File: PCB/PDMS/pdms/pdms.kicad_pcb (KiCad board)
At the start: 2 copper layers, 104 parts, among them IC1 BTS500101TAEATMA1, IC12 TMP126NDCKR, IC13 TMP126NDCKR, IC14 TMP126NDCKR, IC2 BTS500101TAEATMA1, IC3 BTS500101TAEATMA1, IC4 BTS500101TAEATMA1, IC5 BTS500101TAEATMA1, IC6 BTS500101TAEATMA1, IC7 BTS722204ESAXUMA1, IC8 BTS500101TAEATMA1, IC9 BTS500101TAEATMA1, J1 DBG, Q1 AO3401A, Q2 MMBT3904, U1 STM32F405RGTx, U2 MCP2561-E-SN, U3 MCP2561-E-SN, Y1 16Mhz, Y2 32KHz

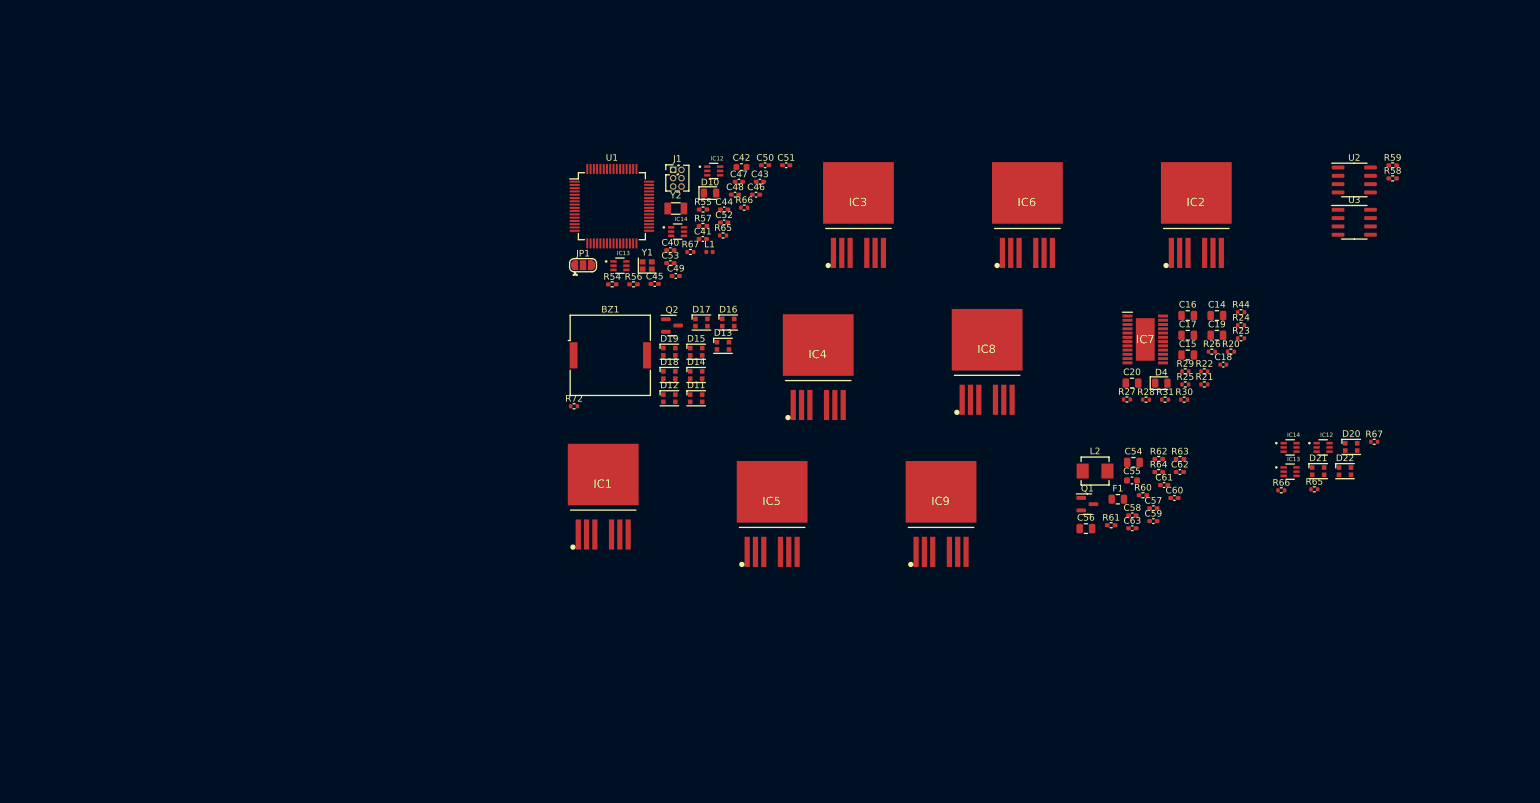
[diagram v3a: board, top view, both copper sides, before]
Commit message: Added ADC overvoltage protection
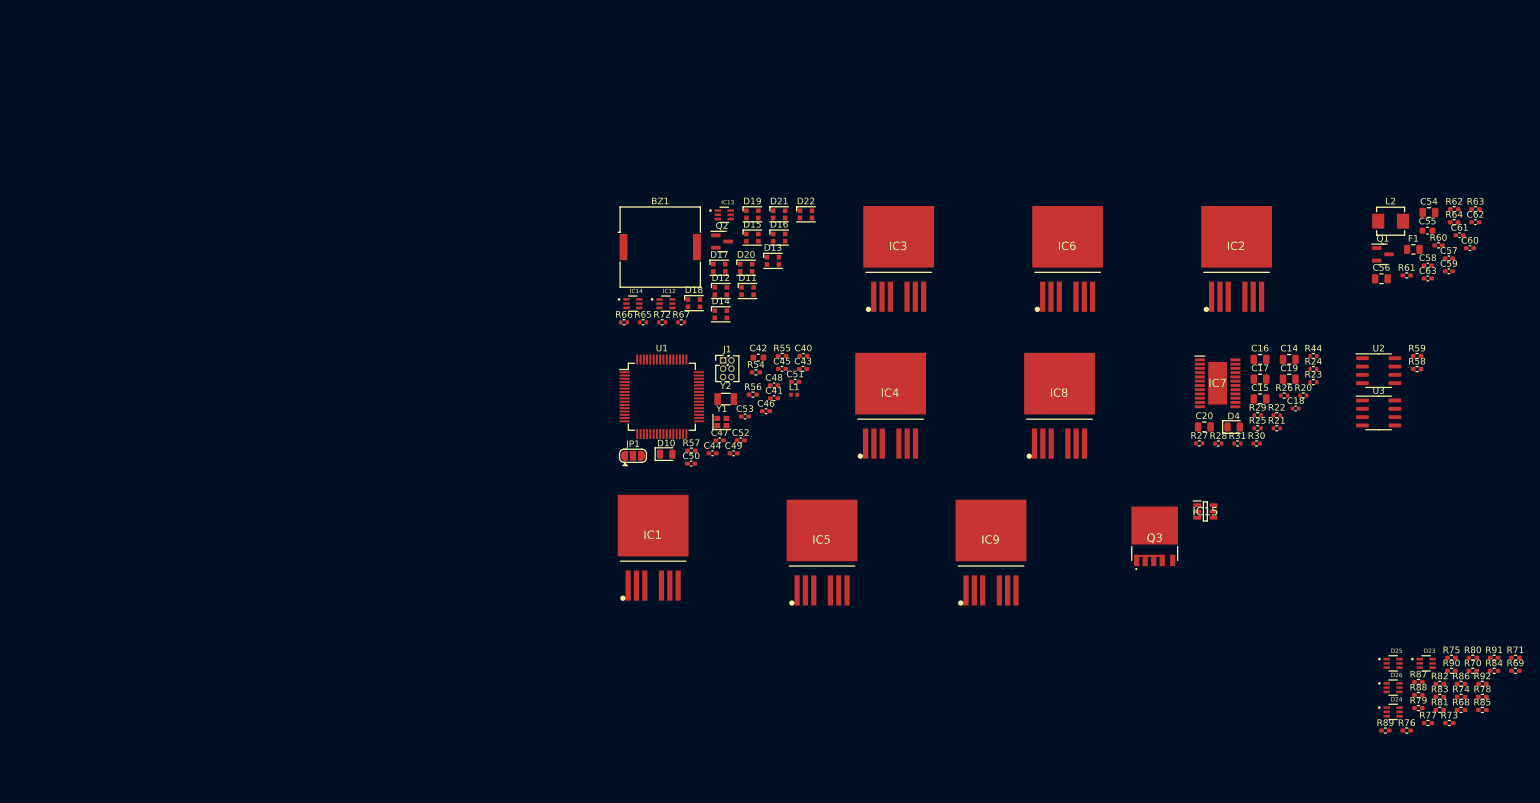
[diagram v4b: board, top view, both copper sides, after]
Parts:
- removed the IC12 at (128.8, 37.9)
- removed the IC12 at (221.8, 80.1)
- removed the IC13 at (114.5, 52.4)
- removed the IC13 at (216.7, 83.8)
- removed the IC14 at (123.3, 47.2)
- removed the IC14 at (216.7, 80.1)
- removed the R65 at (220.4, 86.5)
- removed the R65 at (130.2, 47.8)
- removed the R66 at (133.5, 43.5)
- removed the R66 at (215.4, 86.6)
- removed the R67 at (229.6, 79.2)
- removed the R67 at (125.3, 50.3)
- added D23: BAT54BRW-7-F, PDM_Additional:SOT65P210X110-6N, F.Cu at (237.5, 113.0)
- added D24: BAT54BRW-7-F, PDM_Additional:SOT65P210X110-6N, F.Cu at (232.4, 120.4)
- added D25: BAT54BRW-7-F, PDM_Additional:SOT65P210X110-6N, F.Cu at (232.4, 113.0)
- added D26: BAT54BRW-7-F, PDM_Additional:SOT65P210X110-6N, F.Cu at (232.4, 116.7)
- added IC12: TMP126NDCKR, PDM_Additional:SOT65P210X110-6N, F.Cu at (121.5, 58.2)
- added IC13: TMP126NDCKR, PDM_Additional:SOT65P210X110-6N, F.Cu at (130.4, 44.6)
- added IC14: TMP126NDCKR, PDM_Additional:SOT65P210X110-6N, F.Cu at (116.5, 58.2)
- added IC15: LM74700QDBVRQ1, PDMS_Additional:SOT95P280X145-6N, F.Cu at (203.8, 89.9)
- added Q3: IAUA250N04S6N007AUMA1, PDM_Additional:IAUA250N04S6N007AUMA1, F.Cu at (196.1, 94.9)
- added R65: 10k, Resistor_SMD:R_0402_1005Metric, F.Cu at (118.0, 61.0)
- added R66: 10k, Resistor_SMD:R_0402_1005Metric, F.Cu at (115.1, 61.0)
- added R67: 10k, Resistor_SMD:R_0402_1005Metric, F.Cu at (123.9, 61.0)
- added R68: 1.2k, Resistor_SMD:R_0402_1005Metric_Pad0.72x0.64mm_HandSolder, F.Cu at (242.8, 120.1)
- added R69: 2.2k, Resistor_SMD:R_0402_1005Metric_Pad0.72x0.64mm_HandSolder, F.Cu at (251.1, 114.2)
- added R70: 1.2k, Resistor_SMD:R_0402_1005Metric_Pad0.72x0.64mm_HandSolder, F.Cu at (244.6, 114.2)
- added R71: 2.2k, Resistor_SMD:R_0402_1005Metric_Pad0.72x0.64mm_HandSolder, F.Cu at (251.1, 112.2)
- added R73: 249, Resistor_SMD:R_0402_1005Metric_Pad0.72x0.64mm_HandSolder, F.Cu at (241.0, 122.1)
- added R74: 249, Resistor_SMD:R_0402_1005Metric_Pad0.72x0.64mm_HandSolder, F.Cu at (242.8, 118.1)
- added R75: 1.2k, Resistor_SMD:R_0402_1005Metric_Pad0.72x0.64mm_HandSolder, F.Cu at (241.4, 112.2)
- added R76: 2.2k, Resistor_SMD:R_0402_1005Metric_Pad0.72x0.64mm_HandSolder, F.Cu at (234.5, 123.3)
- added R77: 1.2k, Resistor_SMD:R_0402_1005Metric_Pad0.72x0.64mm_HandSolder, F.Cu at (237.8, 122.1)
- added R78: 2.2k, Resistor_SMD:R_0402_1005Metric_Pad0.72x0.64mm_HandSolder, F.Cu at (246.1, 118.1)
- added R79: 1.2k, Resistor_SMD:R_0402_1005Metric_Pad0.72x0.64mm_HandSolder, F.Cu at (236.3, 119.9)
- added R80: 2.2k, Resistor_SMD:R_0402_1005Metric_Pad0.72x0.64mm_HandSolder, F.Cu at (244.6, 112.2)
- added R81: 1.2k, Resistor_SMD:R_0402_1005Metric_Pad0.72x0.64mm_HandSolder, F.Cu at (239.6, 120.1)
- added R82: 2.2k, Resistor_SMD:R_0402_1005Metric_Pad0.72x0.64mm_HandSolder, F.Cu at (239.6, 116.2)
- added R83: 1.2k, Resistor_SMD:R_0402_1005Metric_Pad0.72x0.64mm_HandSolder, F.Cu at (239.6, 118.1)
- added R84: 2.2k, Resistor_SMD:R_0402_1005Metric_Pad0.72x0.64mm_HandSolder, F.Cu at (247.9, 114.2)
- added R85: 1.2k, Resistor_SMD:R_0402_1005Metric_Pad0.72x0.64mm_HandSolder, F.Cu at (246.1, 120.1)
- added R86: 2.2k, Resistor_SMD:R_0402_1005Metric_Pad0.72x0.64mm_HandSolder, F.Cu at (242.8, 116.2)
- added R87: 249, Resistor_SMD:R_0402_1005Metric_Pad0.72x0.64mm_HandSolder, F.Cu at (236.3, 115.9)
- added R88: 249, Resistor_SMD:R_0402_1005Metric_Pad0.72x0.64mm_HandSolder, F.Cu at (236.3, 117.9)
- added R89: 249, Resistor_SMD:R_0402_1005Metric_Pad0.72x0.64mm_HandSolder, F.Cu at (231.3, 123.3)
- added R90: 249, Resistor_SMD:R_0402_1005Metric_Pad0.72x0.64mm_HandSolder, F.Cu at (241.4, 114.2)
- added R91: 249, Resistor_SMD:R_0402_1005Metric_Pad0.72x0.64mm_HandSolder, F.Cu at (247.9, 112.2)
- added R92: 249, Resistor_SMD:R_0402_1005Metric_Pad0.72x0.64mm_HandSolder, F.Cu at (246.1, 116.2)
- moved D20 96.3 mm to (133.8, 52.7)
- moved D21 91.1 mm to (138.8, 44.5)
- moved D22 91.1 mm to (142.9, 44.5)
- moved C57 59.0 mm to (241.0, 51.2)
- moved C58 59.0 mm to (237.7, 52.3)
- moved C59 59.0 mm to (241.0, 53.2)
- moved C61 59.0 mm to (242.6, 47.7)
- moved C62 59.0 mm to (245.0, 45.7)
- moved C63 59.0 mm to (237.7, 54.3)
- moved R60 59.0 mm to (239.4, 49.3)
- moved C54 59.0 mm to (237.9, 44.3)
- moved C55 59.0 mm to (237.7, 47.0)
- moved C56 59.0 mm to (230.7, 54.4)
- moved C60 59.0 mm to (244.2, 49.7)
- moved F1 59.0 mm to (235.5, 49.9)
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
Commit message: Added CAN ESD protection
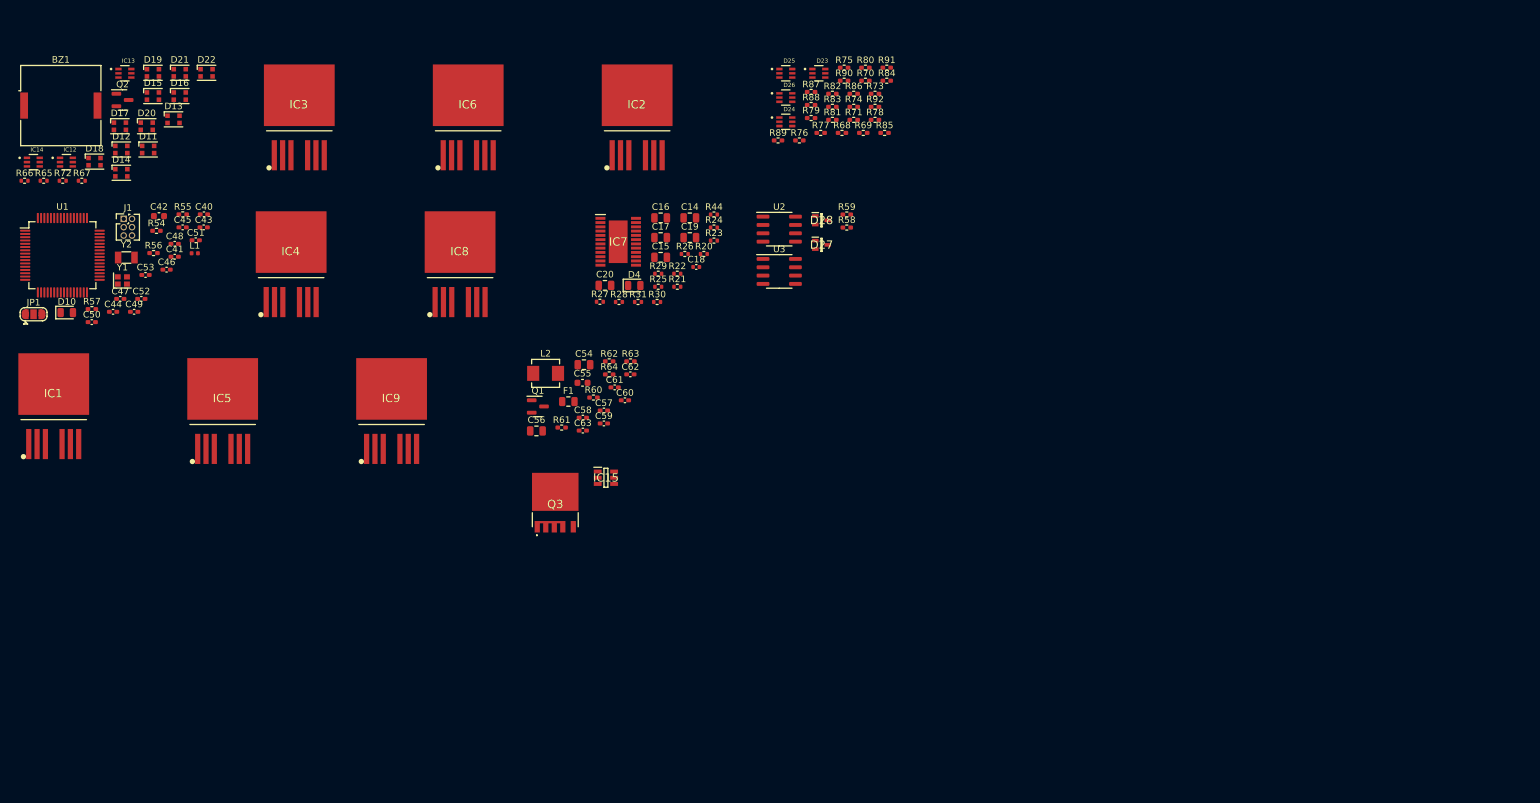
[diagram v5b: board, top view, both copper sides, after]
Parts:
- added D27: PESD2CANFD24L-UX, PDMS_Additional:SOT65P210X110-3N, F.Cu at (145.3, 49.2)
- added D28: PESD2CANFD24L-UX, PDMS_Additional:SOT65P210X110-3N, F.Cu at (145.3, 45.4)
- moved C57 131.0 mm to (112.1, 74.5)
- moved C58 131.0 mm to (108.8, 75.5)
- moved C59 131.0 mm to (112.1, 76.4)
- moved C61 131.0 mm to (113.7, 70.9)
- moved C62 131.0 mm to (116.1, 68.9)
- moved C63 131.0 mm to (108.8, 77.5)
- moved R60 131.0 mm to (110.5, 72.5)
- moved C54 131.0 mm to (109.0, 67.5)
- moved C55 131.0 mm to (108.8, 70.2)
- moved C56 131.0 mm to (101.8, 77.6)
- moved C60 131.0 mm to (115.3, 72.9)
- moved F1 131.0 mm to (106.6, 73.1)
- moved L2 131.0 mm to (103.2, 68.8)
- moved Q1 131.0 mm to (102.0, 73.8)
- moved R61 131.0 mm to (105.6, 77.1)
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
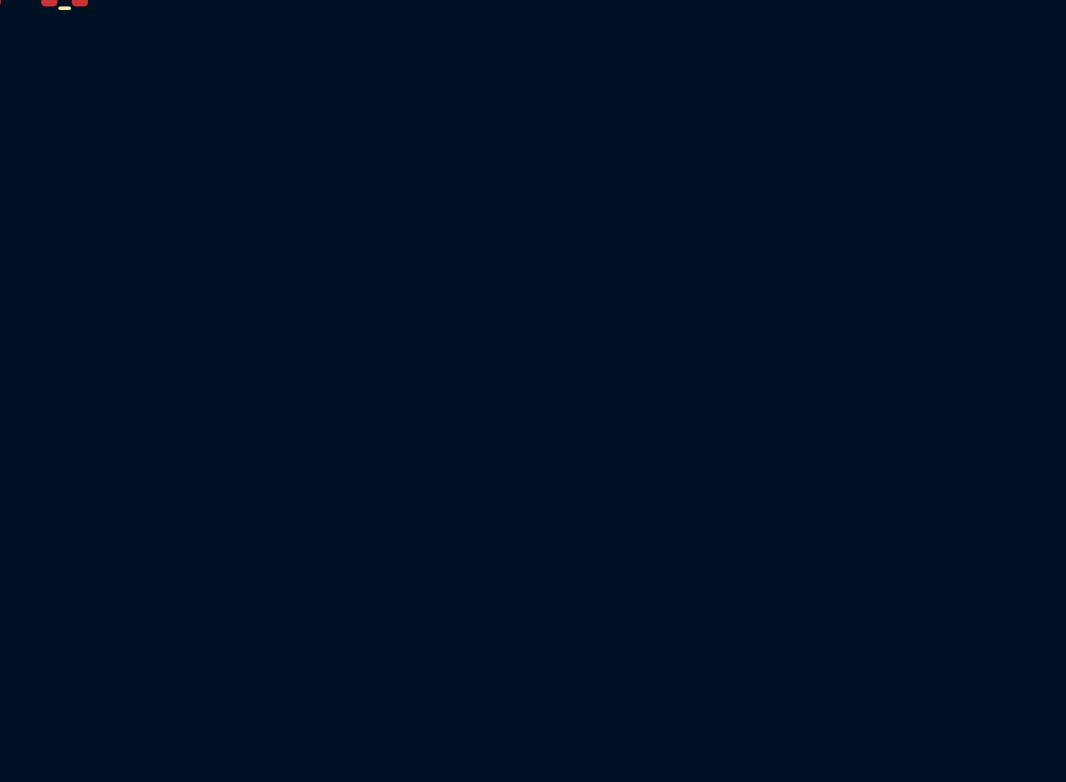
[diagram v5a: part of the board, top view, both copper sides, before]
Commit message: Modified power switch section - partly finished
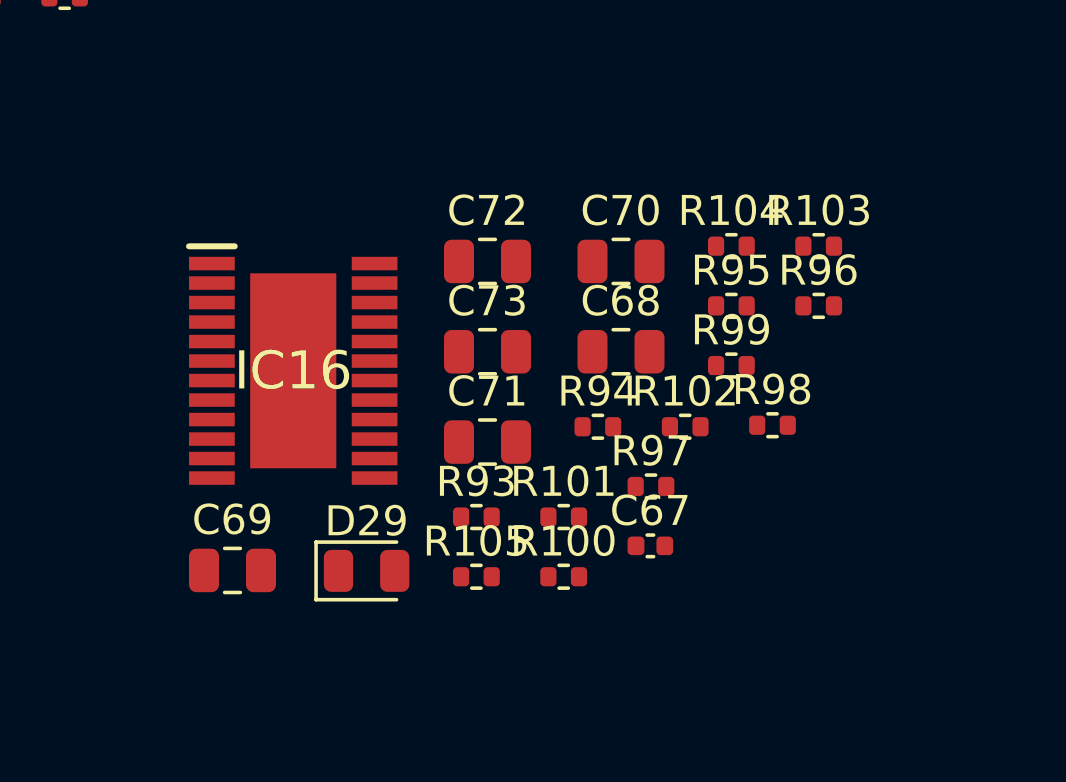
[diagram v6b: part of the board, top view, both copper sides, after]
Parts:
- added C67: 220pF, Capacitor_SMD:C_0402_1005Metric, F.Cu at (139.7, 76.2)
- added C68: 470nF, Capacitor_SMD:C_0805_2012Metric, F.Cu at (138.7, 69.7)
- added C69: 100nF, Capacitor_SMD:C_0805_2012Metric, F.Cu at (125.8, 77.0)
- added C70: 10nf, Capacitor_SMD:C_0805_2012Metric, F.Cu at (138.7, 66.7)
- added C71: 10nf, Capacitor_SMD:C_0805_2012Metric, F.Cu at (134.3, 72.7)
- added C72: 10nf, Capacitor_SMD:C_0805_2012Metric, F.Cu at (134.3, 66.7)
- added C73: 10nf, Capacitor_SMD:C_0805_2012Metric, F.Cu at (134.3, 69.7)
- added D29: 7V, Diode_SMD:D_0805_2012Metric, F.Cu at (130.2, 77.0)
- added IC16: BTS722204ESAXUMA1, PDM_Additional:SOP65P600X115-25N, F.Cu at (127.8, 70.4)
- added R100: 1.2k, Resistor_SMD:R_0402_1005Metric, F.Cu at (136.8, 77.2)
- added R101: 4.7k, Resistor_SMD:R_0402_1005Metric, F.Cu at (136.8, 75.2)
- added R102: 4.7k, Resistor_SMD:R_0402_1005Metric, F.Cu at (140.9, 72.2)
- added R103: 4.7k, Resistor_SMD:R_0402_1005Metric, F.Cu at (145.3, 66.2)
- added R104: 4.7k, Resistor_SMD:R_0402_1005Metric, F.Cu at (142.4, 66.2)
- added R105: 1.2k, Resistor_SMD:R_0402_1005Metric, F.Cu at (133.9, 77.2)
- added R93: 1.2k, Resistor_SMD:R_0402_1005Metric, F.Cu at (133.9, 75.2)
- added R94: 47, Resistor_SMD:R_0402_1005Metric, F.Cu at (137.9, 72.2)
- added R95: 470, Resistor_SMD:R_0402_1005Metric, F.Cu at (142.4, 68.2)
- added R96: 4.7k, Resistor_SMD:R_0402_1005Metric, F.Cu at (145.3, 68.2)
- added R97: 1.2k, Resistor_SMD:R_0402_1005Metric, F.Cu at (139.7, 74.2)
- added R98: 1.2k, Resistor_SMD:R_0402_1005Metric, F.Cu at (143.8, 72.2)
- added R99: 1.2k, Resistor_SMD:R_0402_1005Metric, F.Cu at (142.4, 70.2)
